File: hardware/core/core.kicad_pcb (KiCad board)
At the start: 2 copper layers, 23 x 32 mm, 35 parts, among them J1 MOLEX_SlimStack_505550-1020, U1 XIAO-NRF54L15, U2 BQ25173DSG, U3 BQ25570, U5 AXP1T34

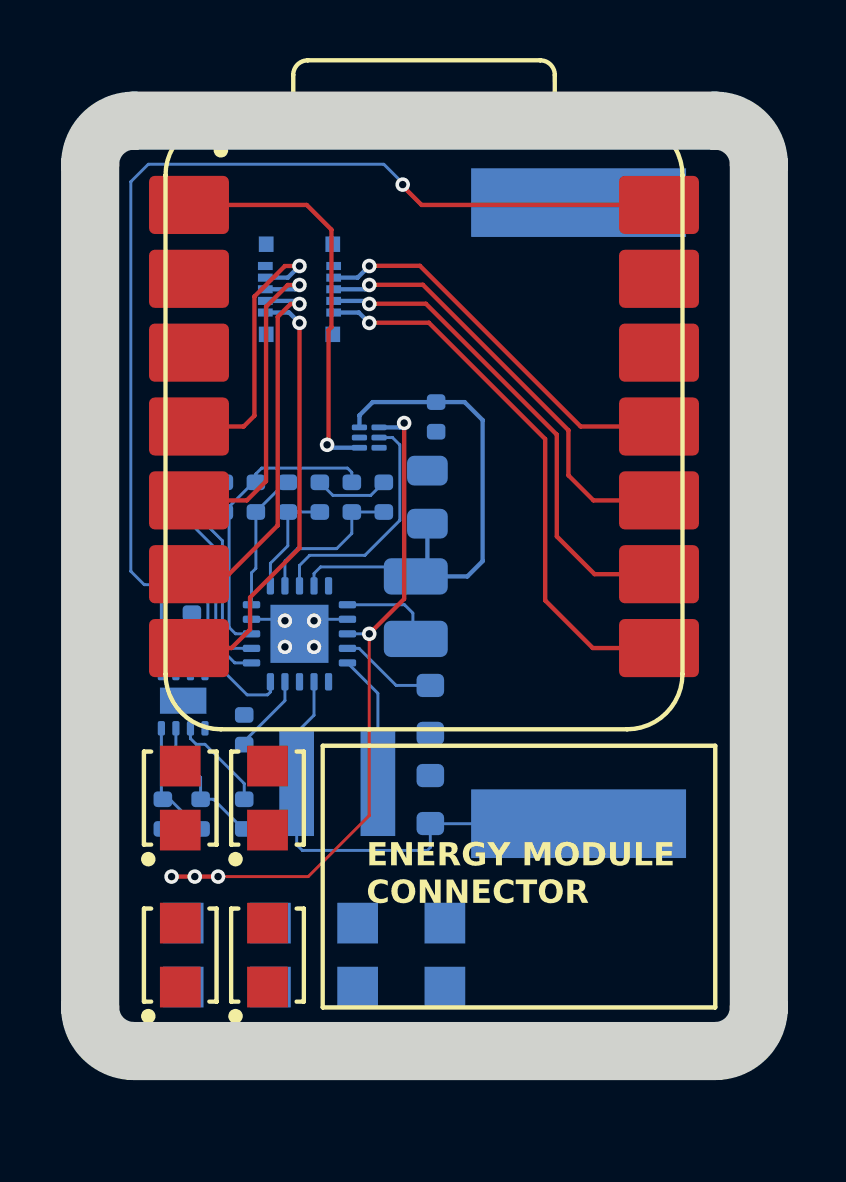
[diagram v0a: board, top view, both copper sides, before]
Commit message: Initial pass at routing main circuit components
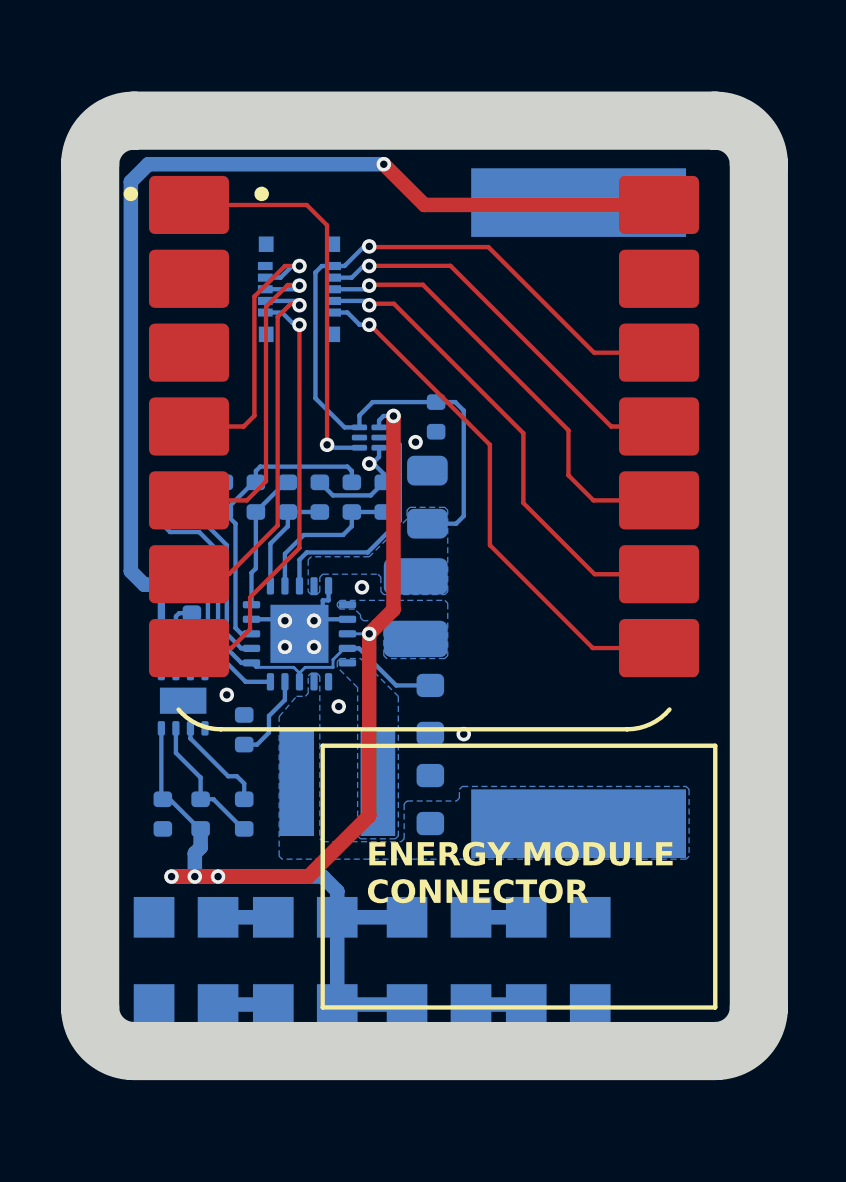
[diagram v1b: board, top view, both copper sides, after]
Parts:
- Cb3, Cb4, Cb6, Cb8: moved to B.Cu
- moved Cb6 10.1 mm to (95.1, 77.4), turned to 0 degrees
- moved Cb1 6.04 mm to (91.0, 80.4), turned to 0 degrees
- moved Cb7 4.53 mm to (86.4, 80.4), turned to 180 degrees
- moved Cb3 4.30 mm to (86.4, 77.4), turned to 180 degrees
- moved Cb2 4.25 mm to (95.1, 80.4), turned to 0 degrees
- moved Cb4 4.10 mm to (82.3, 77.4), turned to 180 degrees
- moved Cb5 3.09 mm to (91.0, 77.4), turned to 0 degrees
- moved Cb8 1.71 mm to (82.3, 80.4), turned to 180 degrees
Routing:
- net VCAP: track 27.5 -> 43.8 mm
- net /harvester/VIN_DC: track 16.5 -> 1.70 mm
- net +3V3: track 18.5 -> 29.8 mm, vias 0 -> 1
- net GND: track 6.39 -> 11.5 mm, vias 4 -> 10
- net /harvester/LBOOST: track 4.53 -> 0.00 mm
- net /harvester/VSTOR: track 10.8 -> 14.9 mm
- net /harvester/LBUCK: track 3.26 -> 0.00 mm
- net Net-(Cb5-Pad2): track 0.00 -> 1.90 mm
- net Net-(Cb1-Pad2): track 0.00 -> 1.90 mm
- net Net-(Cb7-Pad2): track 0.00 -> 1.90 mm
- net Net-(Cb3-Pad2): track 0.00 -> 1.90 mm
- net /system/RX: track 19.2 -> 18.0 mm
- net VUSB: track 43.9 -> 43.0 mm
- net /system/SPI_CLK: track 17.1 -> 16.5 mm
- added copper zone on B.Cu, net +3V3
- added copper zone on B.Cu, net /harvester/LBOOST
- added copper zone on B.Cu, net /harvester/LBUCK
- added copper zone on B.Cu, net /harvester/VIN_DC
- added copper zone on B.Cu, net GND
- added copper zone on F.Cu, net GND
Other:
- board text removed: "CAPS?"

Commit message: Updated with cap and connector
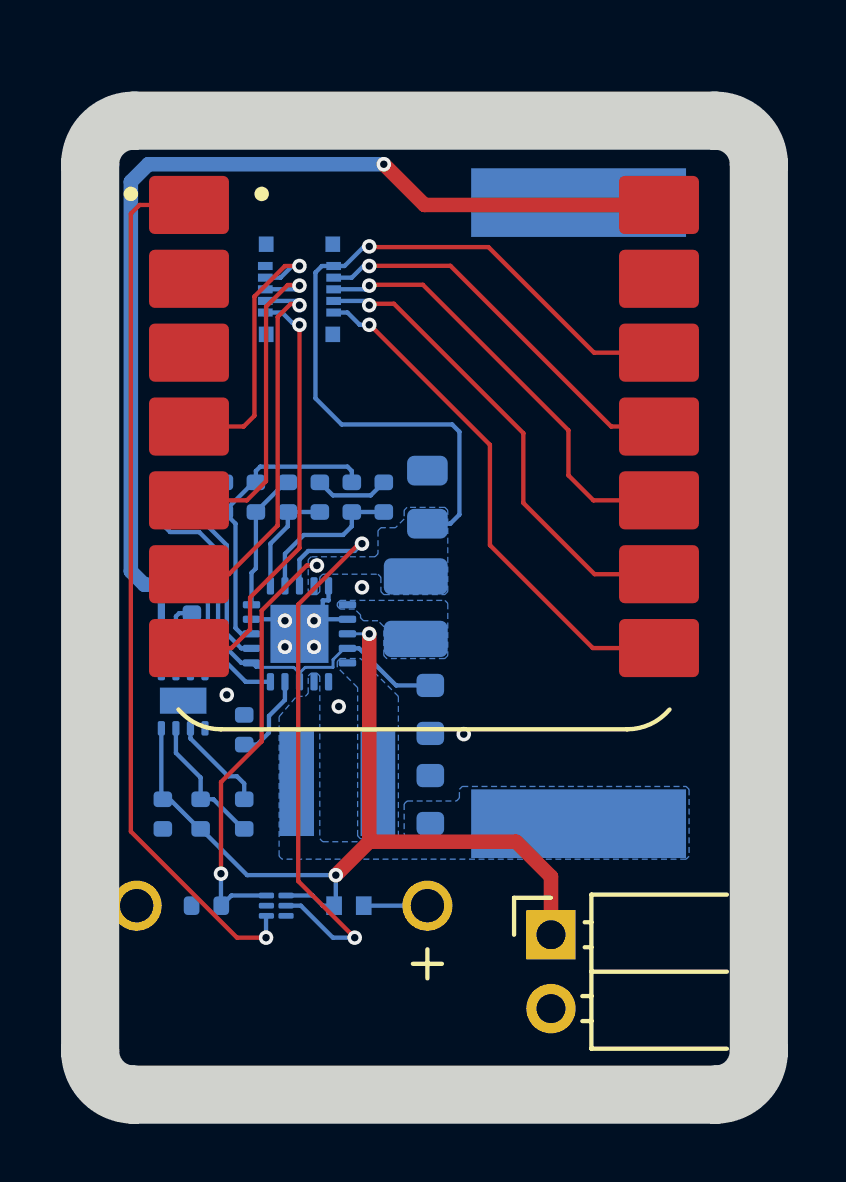
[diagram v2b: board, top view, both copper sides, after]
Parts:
- removed Cb2, Cb3, Cb4, Cb5, Cb6, Cb7, Cb8: 11m, part_specific:SEIKO_CPH3225A
- added J2: Conn_01x02_Pin, connectors:PinHeader_1x02_P2.54mm_Horizontal, F.Cu at (94.8, 78.0)
- added JP1: SolderJumper_2_Open, misc:SolderJumper2_Open_0402, B.Cu at (87.9, 77.0)
- Cb1: value 11m -> 470m; footprint part_specific:SEIKO_CPH3225A -> part_specific:EATON_KR5R5H474R; moved to F.Cu
- moved C8 18.6 mm to (83.0, 77.0), turned to 180 degrees
- moved U5 16.4 mm to (85.4, 77.0)
- moved Cb1 10.9 mm to (80.6, 77.0), turned to 180 degrees
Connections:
- Cb1 pad 1: VCAP -> /harvester/CAP_J
- Cb1 pad 2: Net-(Cb1-Pad2) -> GND
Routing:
- net /harvester/VBAT_OK_MCU: track 13.7 -> 30.3 mm
- net +3V3: track 29.8 -> 43.1 mm, vias 1 -> 3
- net VCAP: track 43.8 -> 30.6 mm, vias 5 -> 2
- net /harvester/VBAT_OK: track 8.33 -> 21.4 mm, vias 0 -> 2
- net /harvester/CAP_J: track 0.00 -> 2.19 mm
- net Net-(Cb5-Pad2): track 1.90 -> 0.00 mm
- net Net-(Cb1-Pad2): track 1.90 -> 0.00 mm
- net Net-(Cb7-Pad2): track 1.90 -> 0.00 mm
- net Net-(Cb3-Pad2): track 1.90 -> 0.00 mm
- net GND: track 11.5 -> 9.80 mm, vias 10 -> 8
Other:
- board size 23 x 32 mm -> 23 x 33.5 mm
- board text removed: "ENERGY MODULE CONNECTOR"

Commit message: updated layout with footprint changes
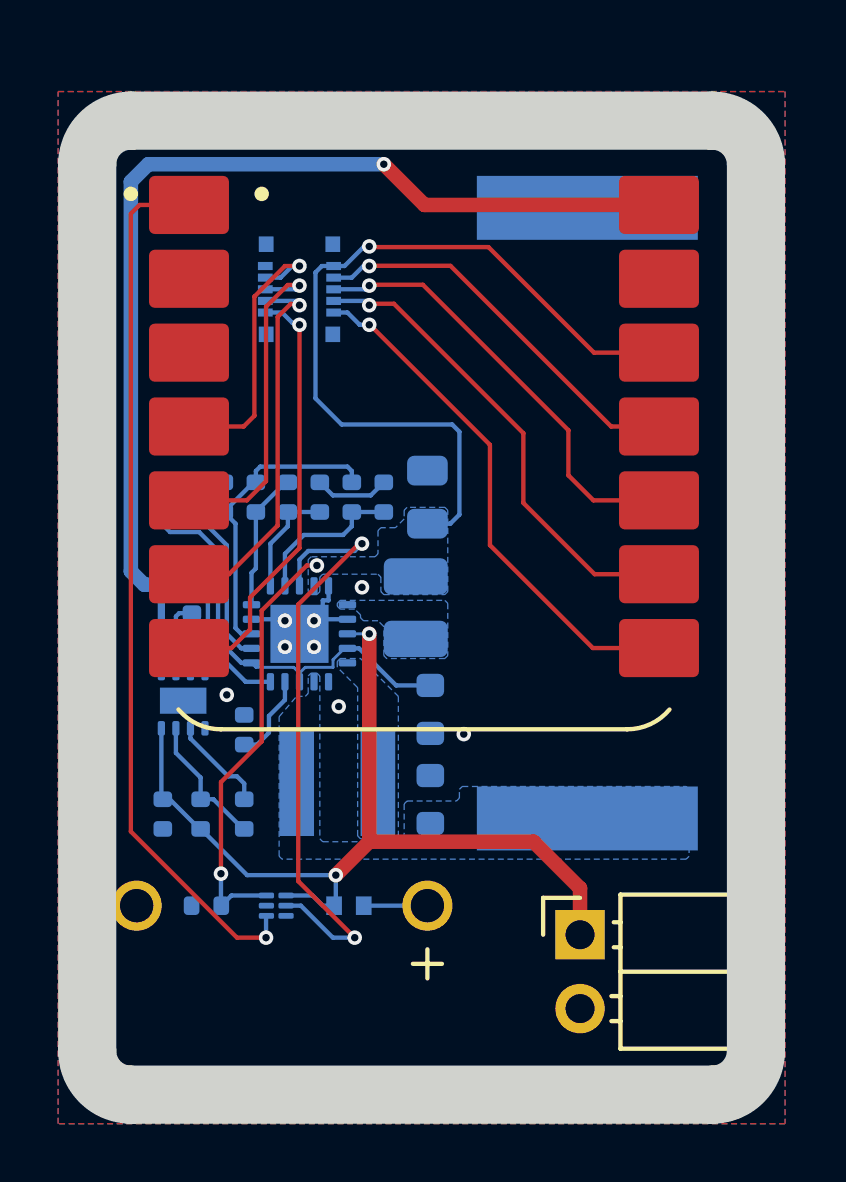
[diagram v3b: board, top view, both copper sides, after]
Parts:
- moved J2 1.00 mm to (95.8, 78.0)
- moved SC1 0.30 mm to (96.1, 63.5)
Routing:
- net VCAP: track 30.6 -> 31.4 mm

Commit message: bom updates
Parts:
- J2: footprint connectors:PinHeader_1x02_P2.54mm_Horizontal -> connectors:PD_801-83-002-20-001101
- moved Cb1 6.65 mm to (87.2, 77.0), turned to 0 degrees
- moved J2 1.60 mm to (94.6, 77.0)
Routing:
- net VCAP: track 31.4 -> 29.7 mm
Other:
- board size 23 x 33.5 mm -> 23 x 33 mm
- board text added: "${TITLE} V${REVISION}"

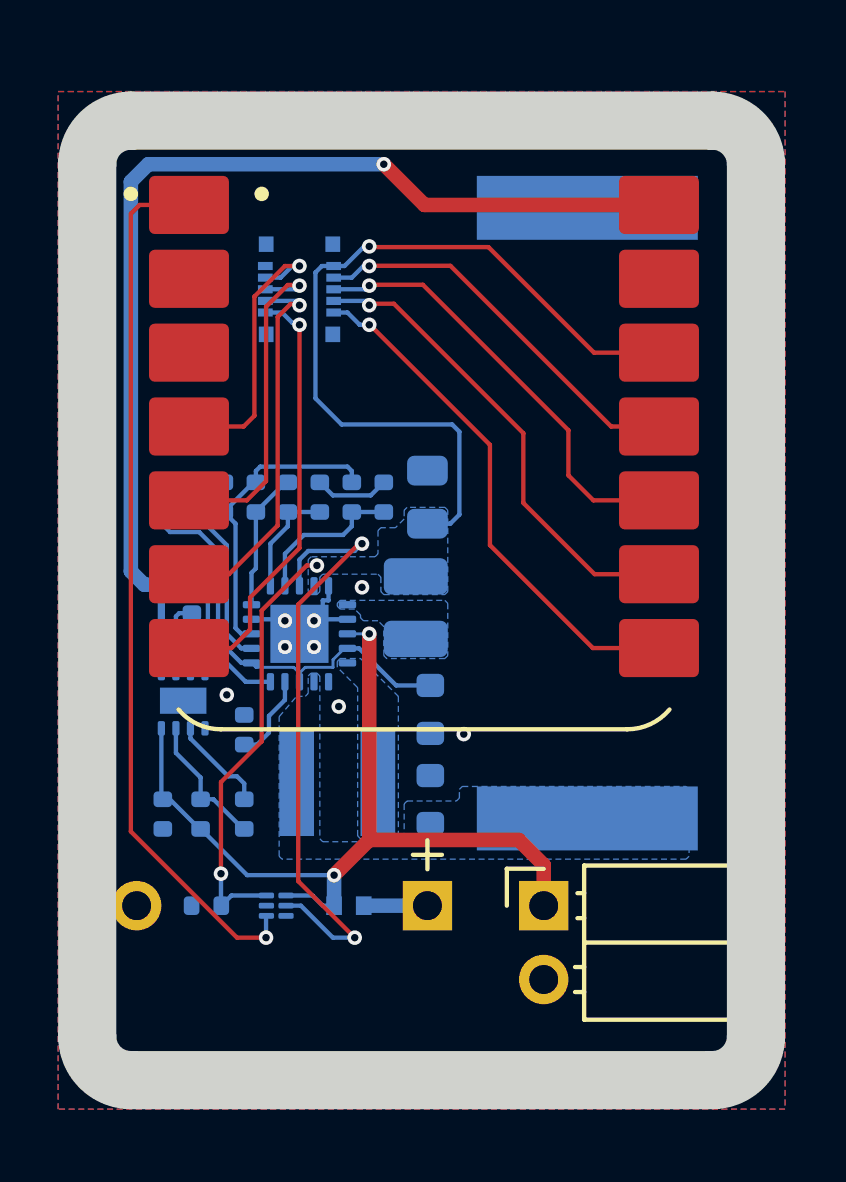
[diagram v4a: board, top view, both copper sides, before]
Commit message: updated harvester configuration resistors and removed cap solder link
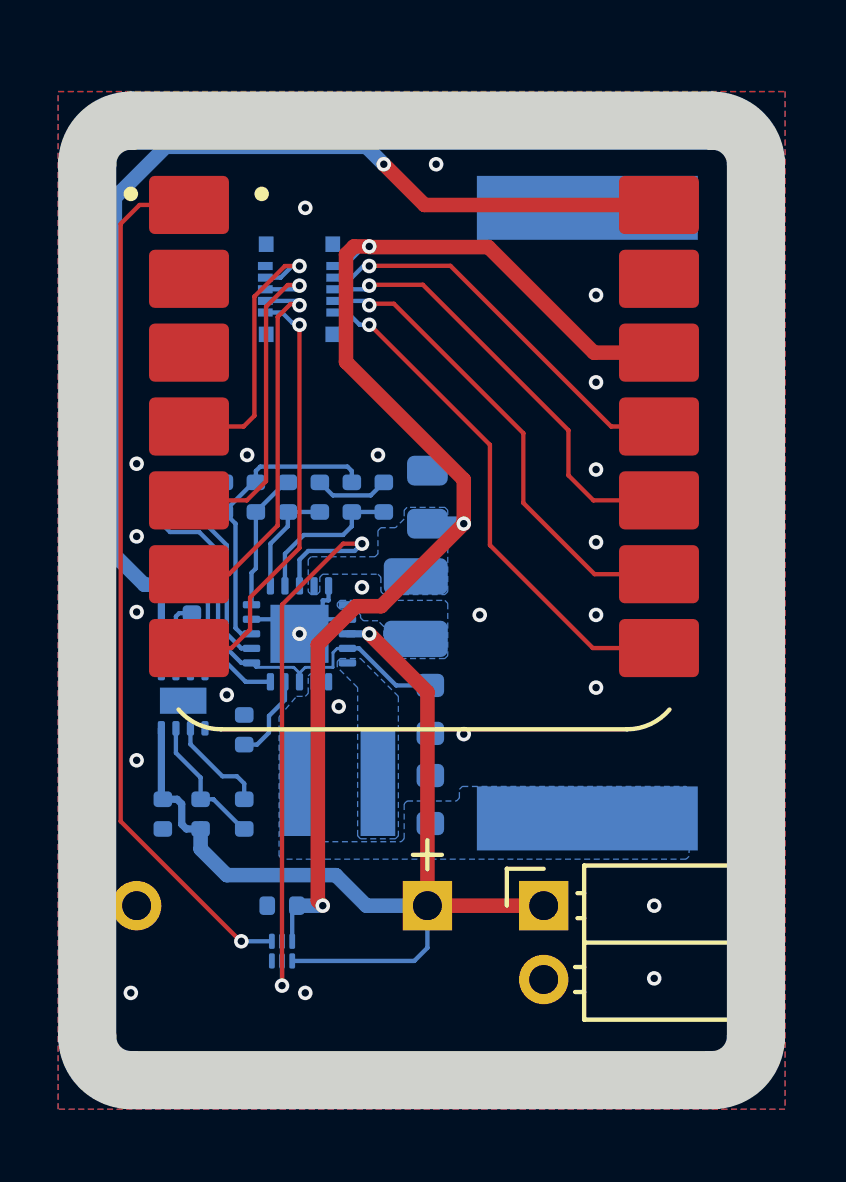
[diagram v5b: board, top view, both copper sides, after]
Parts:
- removed JP1: SolderJumper_2_Open, misc:SolderJumper2_Open_0402
- ROK1: value 5.6M -> 4.7M
- ROK2: value 4.7M -> 5.1M
- ROK3: value 1.2M -> 3.0M
- ROUT1: value 4.7M -> 6.49
- ROUT2: value 8.2M -> 6.49
- ROV1: value 4.3M -> 4.22M
- moved C8 2.60 mm to (85.6, 77.0)
- moved U5 1.58 mm to (85.6, 78.6), turned to 90 degrees
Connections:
- Cb1 pad 1: /harvester/CAP_J -> VCAP
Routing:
- net VCAP: track 29.7 -> 35.1 mm, vias 2 -> 1
- net /harvester/CAP_J: track 2.19 -> 0.00 mm
- net +3V3: track 43.1 -> 44.6 mm
- net VUSB: track 43.0 -> 43.9 mm
- net /harvester/VBAT_OK: track 21.4 -> 20.8 mm
- net GND: track 9.80 -> 10.1 mm, vias 8 -> 24

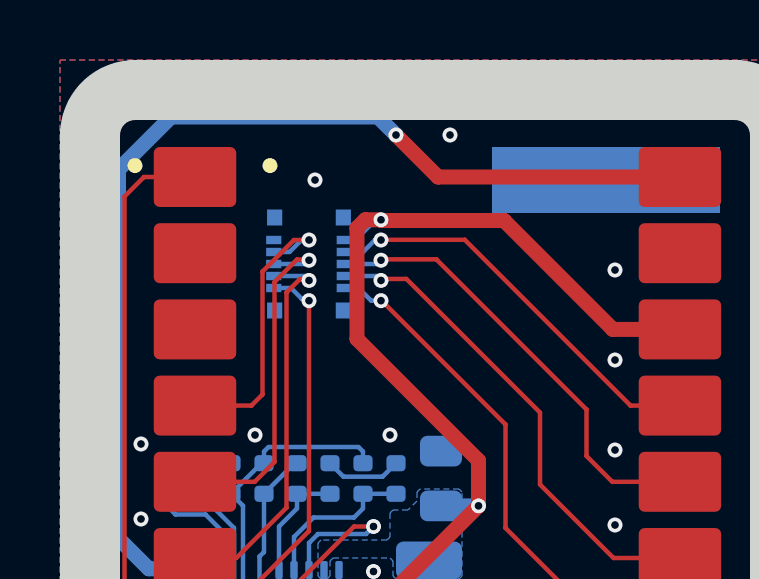
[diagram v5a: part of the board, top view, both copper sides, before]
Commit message: corrected pin mating to sensor module
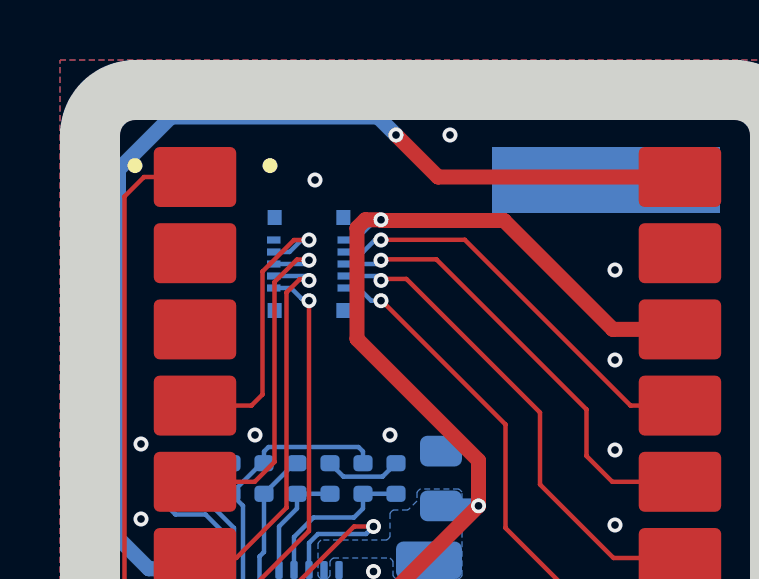
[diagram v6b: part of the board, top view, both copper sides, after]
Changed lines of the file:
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@@
 			(end 2.2479 1.3462)
 			(stroke
-				(width 0.0254)
+				(width 0.05)
 				(type solid)
 			)
@@
 			(end 2.2479 -1.3462)
 			(stroke
-				(width 0.0254)
+				(width 0.05)
 				(type solid)
 			)
@@
 			(end -2.2479 1.3462)
 			(stroke
-				(width 0.0254)
+				(width 0.05)
 				(type solid)
 			)
@@
 			(end -2.2479 -1.3462)
 			(stroke
-				(width 0.0254)
+				(width 0.05)
 				(type solid)
 			)
@@
 		(pad "1" smd rect
 			(at -0.800001 1.174999 90)
-			(size 0.2794 0.508)
+			(size 0.24 0.45)
 			(layers "B.Cu" "B.Mask" "B.Paste")
 			(net 29 "/system/RX")
@@
 		(pad "2" smd rect
 			(at -0.800001 -1.174999 90)
-			(size 0.2794 0.508)
+			(size 0.24 0.45)
 			(layers "B.Cu" "B.Mask" "B.Paste")
 			(net 27 "/system/TX")
@@
 		(pad "3" smd rect
 			(at -0.399999 1.174999 90)
-			(size 0.2794 0.508)
+			(size 0.24 0.45)
 			(layers "B.Cu" "B.Mask" "B.Paste")
 			(net 22 "/system/SPI_CLK")
@@
 		(pad "4" smd rect
 			(at -0.399999 -1.174999 90)
-			(size 0.2794 0.508)
+			(size 0.24 0.45)
 			(layers "B.Cu" "B.Mask" "B.Paste")
 			(net 26 "/system/I2C_SCL")
@@
 		(pad "5" smd rect
 			(at 0 1.174999 90)
-			(size 0.2794 0.508)
+			(size 0.24 0.45)
 			(layers "B.Cu" "B.Mask" "B.Paste")
 			(net 24 "/system/SPI_MISO")
@@
 		(pad "6" smd rect
 			(at 0 -1.174999 90)
-			(size 0.2794 0.508)
+			(size 0.24 0.45)
 			(layers "B.Cu" "B.Mask" "B.Paste")
 			(net 28 "/system/I2C_SDA")
@@
 		(pad "7" smd rect
 			(at 0.399999 1.174999 90)
-			(size 0.2794 0.508)
+			(size 0.24 0.45)
 			(layers "B.Cu" "B.Mask" "B.Paste")
 			(net 23 "/system/SPI_MOSI")
@@
 		(pad "8" smd rect
 			(at 0.399999 -1.174999 90)
-			(size 0.2794 0.508)
+			(size 0.24 0.45)
 			(layers "B.Cu" "B.Mask" "B.Paste")
 			(net 25 "/system/ANA3")
@@
 		(pad "9" smd rect
 			(at 0.800001 1.174999 90)
-			(size 0.2794 0.508)
+			(size 0.24 0.45)
 			(layers "B.Cu" "B.Mask" "B.Paste")
 			(net 4 "+3V3")
@@
 		(pad "10" smd rect
 			(at 0.800001 -1.174999 90)
-			(size 0.2794 0.508)
+			(size 0.24 0.45)
 			(layers "B.Cu" "B.Mask" "B.Paste")
 			(net 2 "GND")
@@
 		(pad "MP" smd rect
 			(at -1.550035 -1.144999 90)
-			(size 0.5334 0.508)
+			(size 0.5 0.47)
 			(layers "B.Cu" "B.Mask" "B.Paste")
 			(net 2 "GND")
@@
 		(pad "MP" smd rect
 			(at -1.549999 1.144999 90)
-			(size 0.5334 0.508)
+			(size 0.5 0.47)
 			(layers "B.Cu" "B.Mask" "B.Paste")
 			(net 2 "GND")
@@
 		(pad "MP" smd rect
 			(at 1.549999 1.144999 90)
-			(size 0.5334 0.508)
+			(size 0.5 0.47)
 			(layers "B.Cu" "B.Mask" "B.Paste")
 			(net 2 "GND")
@@
 		(pad "MP" smd rect
 			(at 1.550035 -1.144999 90)
-			(size 0.5334 0.508)
+			(size 0.5 0.47)
 			(layers "B.Cu" "B.Mask" "B.Paste")
 			(net 2 "GND")
